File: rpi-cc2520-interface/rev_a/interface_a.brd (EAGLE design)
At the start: 30.5 x 39.5 mm, 5 parts, among them J1 PINHD-2X12/SMD, J2 PINHD-2X12/SMD

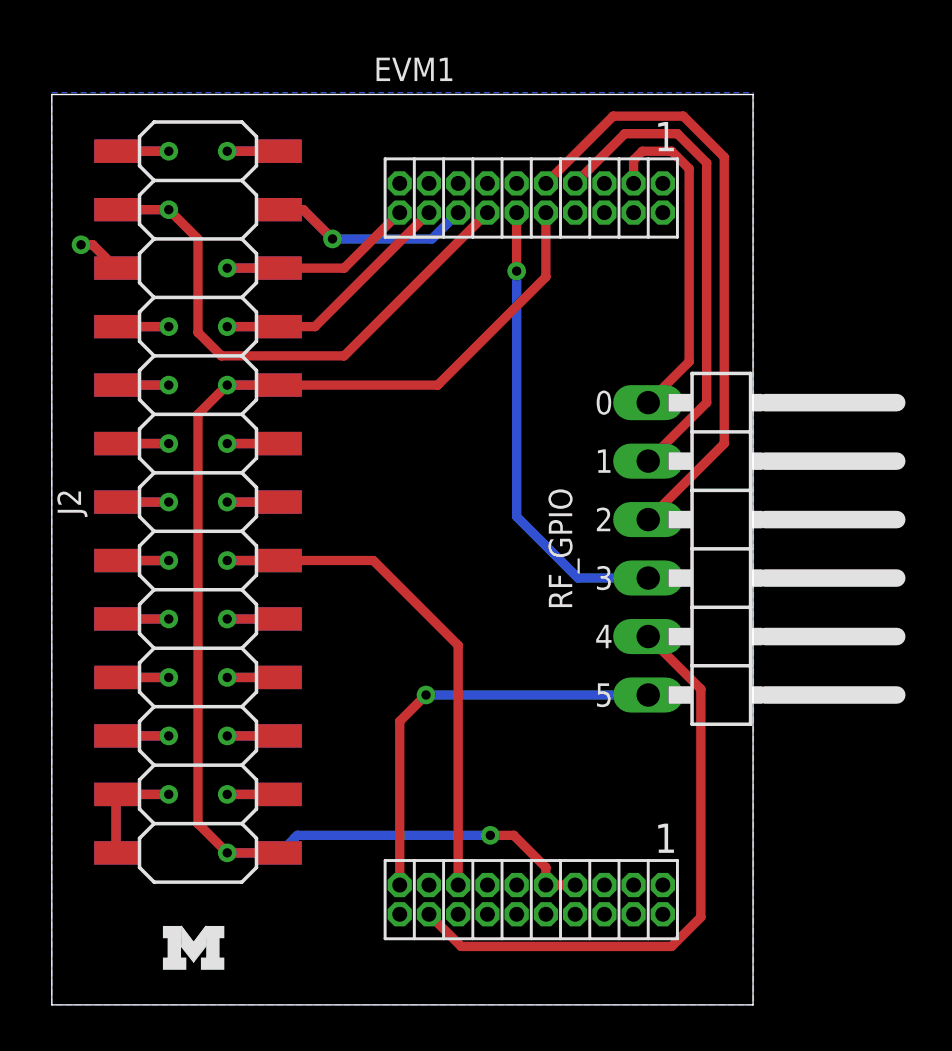
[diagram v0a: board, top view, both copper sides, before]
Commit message: cleaned up traces and added silkscreen to rpi-2520 interface board
git-svn-id: svn+ssh://energy.eecs.umich.edu/svnroot/shed/projects/pi-router/eagle@1701 d5a83394-2863-40c7-9603-03341d4c7fdc
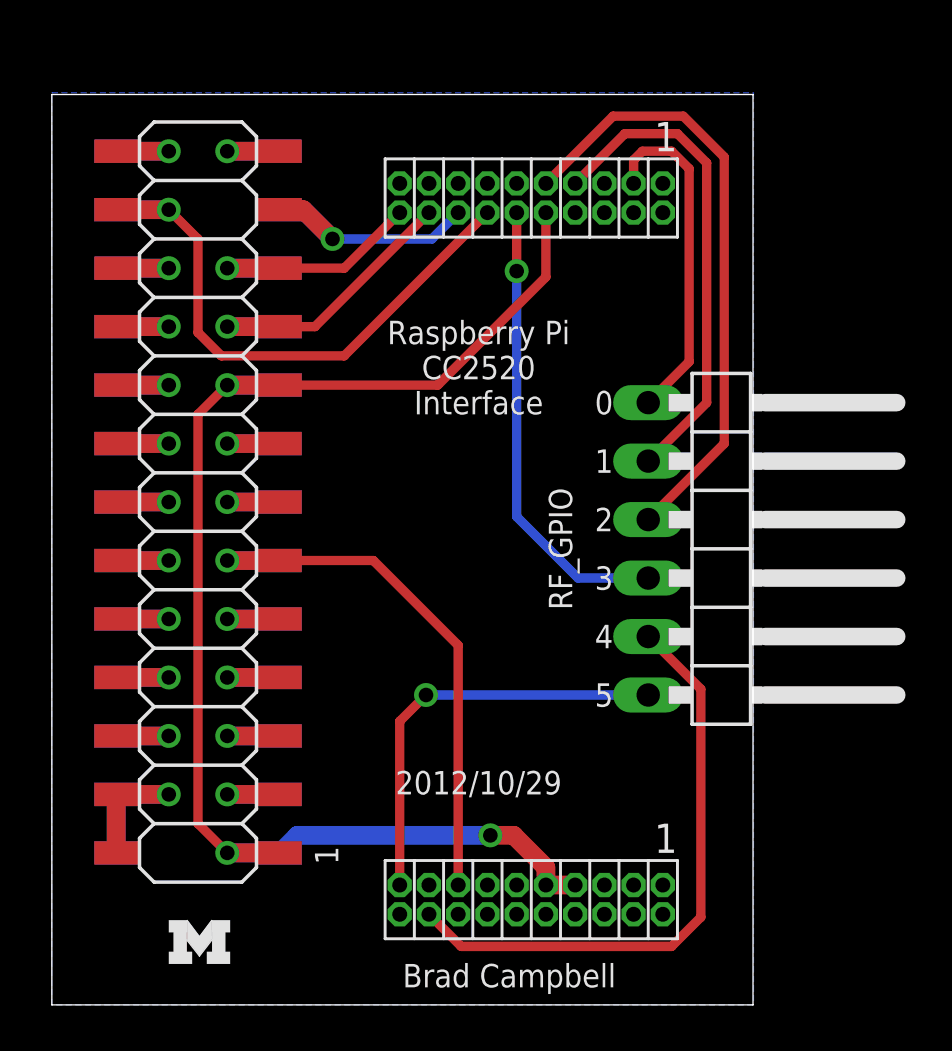
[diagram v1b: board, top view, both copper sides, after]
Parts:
- moved U$1 0.36 mm to (5.08, 1.78)
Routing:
- net GPIO25: track 3.89 -> 4.57 mm
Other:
- board text added: "2012/10/29"
- board text added: "Brad Campbell"
- board text added: "Raspberry Pi CC2520 Interface"
